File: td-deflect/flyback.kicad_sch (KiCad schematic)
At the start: 38 parts, among them Q12 G3R450MT17J, U13 MCP1416

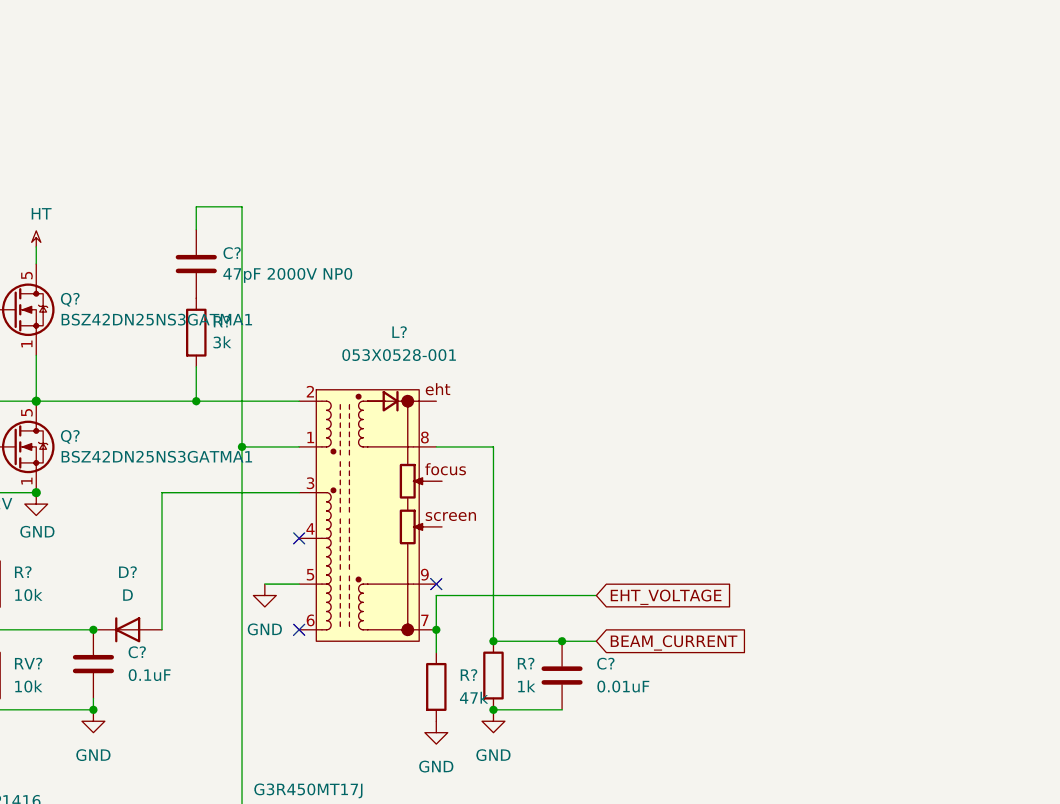
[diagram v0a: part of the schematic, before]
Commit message: modify flyback feedback mechanism
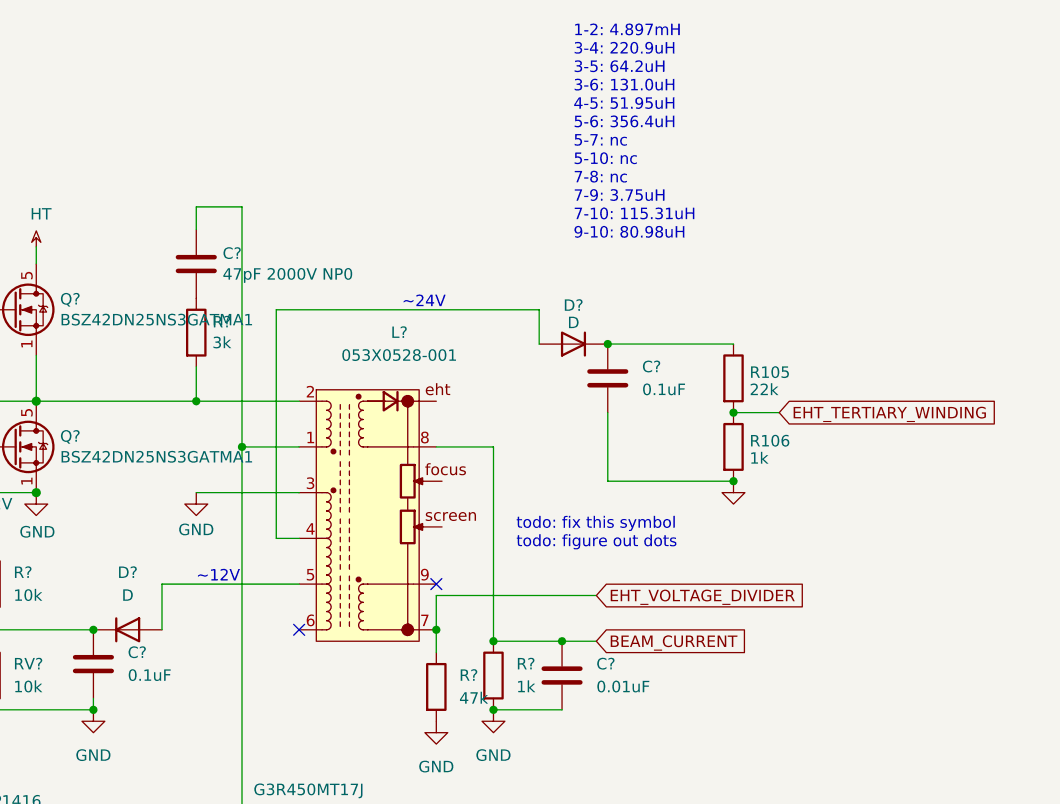
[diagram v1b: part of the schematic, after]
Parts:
- added C?: 0.1uF, symbol Device:C
- added D?: D, symbol Device:D
- added R105: 22k, symbol Device:R
- added R106: 1k, symbol Device:R
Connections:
- net GND: now also L?.3, C?.2, R106.2; no longer L?.5
- net at D?.2 (A): now also L?.5; no longer L?.3
- net at L?.4: now also D?.2 (A)
- net EHT_VOLTAGE renamed EHT_VOLTAGE_DIVIDER
- new net: C?.1, D?.1 (K), R105.1
- new net EHT_TERTIARY_WINDING: R105.2, R106.1
- no-connect marks 3 -> 2
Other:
- note added: "1-2: 4.897mH 3-4: 220.9uH 3-5: 64.2uH 3-6: 131.0uH 4-5: 51.95uH 5-6: 356.4uH 5-7: nc 5-10: nc 7-8: nc 7-9: 3.75uH 7-10: 115.31uH 9-10: 80.98uH"
- note added: "todo: fix this symbol todo: figure out dots"
- note added: "~12V"
- note added: "~24V"

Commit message: more updates
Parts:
- added TP10, TP11, TP4, TP5, TP6, TP7, TP8, TP9: TestPoint, TestPoint:TestPoint_Keystone_5010-5014_Multipurpose, symbol Connector:TestPoint
- C? (x4): footprint (none) -> Capacitor_SMD:C_0805_2012Metric_Pad1.15x1.40mm_HandSolder
- R105, R106, R? (x5): footprint (none) -> Resistor_SMD:R_0805_2012Metric_Pad1.15x1.40mm_HandSolder
- RV?: footprint (none) -> Potentiometer_THT:Potentiometer_Bourns_3386P_Vertical
- U? (x3): footprint (none) -> Package_SO:SOIC-8_3.9x4.9mm_P1.27mm
- U? (x3): footprint (none) -> Package_SO:SOIC-14_3.9x8.7mm_P1.27mm
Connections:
- net BEAM_CURRENT: now also TP6.1
- net EHT_FLYBACK_VOLTAGE: now also TP4.1
- net EHT_VOLTAGE_DIVIDER: now also TP7.1
- net at C?.1, D?.1 (K), U?.2 (-)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: now also TP10.1
- net at R?.2, U?.1, U?.1: now also TP5.1
- net at C?.1, D?.1 (K), R105.1: now also TP9.1
- net at D?.2 (A), L?.4: now also TP8.1
- net at U13.3 (IN), U?.3: now also TP11.1

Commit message: even more updates
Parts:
- L?: footprint (none) -> td-hv:053X0528-001
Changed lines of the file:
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@@
       (effects (font (size 1.27 1.27)))
     )
-    (property "Footprint" "" (at 159.385 61.595 90)
+    (property "Footprint" "td-hv:053X0528-001" (at 159.385 61.595 90)
       (effects (font (size 1.27 1.27)) hide)
     )

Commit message: small bugfix
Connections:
- net EHT_FLYBACK_CURRENT: now also Q12.2 (DS)
- net GND: no longer Q12.2 (DS)
- net HV_PROTECT: now reaches D?.1 (K), U?.1
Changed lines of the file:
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@@
   (junction (at 203.2 118.11) (diameter 0) (color 0 0 0 0)
   )
-  (junction (at 127 120.65) (diameter 0) (color 0 0 0 0)
+  (junction (at 96.52 101.6) (diameter 0) (color 0 0 0 0)
   )
   (junction (at 102.87 113.03) (diameter 0) (color 0 0 0 0)
@@
   )
   (junction (at 171.45 87.63) (diameter 0) (color 0 0 0 0)
+  )
+  (junction (at 142.24 118.11) (diameter 0) (color 0 0 0 0)
   )
   (junction (at 114.3 92.71) (diameter 0) (color 0 0 0 0)
@@
     (stroke (width 0) (type default))
   )
+  (wire (pts (xy 142.24 118.11) (xy 149.86 118.11))
+    (stroke (width 0) (type default))
+  )
   (wire (pts (xy 110.49 49.53) (xy 113.03 49.53))
     (stroke (width 0) (type solid))
@@
     (stroke (width 0) (type default))
   )
-  (wire (pts (xy 127 120.65) (xy 133.35 120.65))
-    (stroke (width 0) (type default))
-  )
   (wire (pts (xy 111.76 104.14) (xy 113.03 104.14))
     (stroke (width 0) (type default))
@@
     (stroke (width 0) (type default))
   )
+  (wire (pts (xy 142.24 115.57) (xy 142.24 118.11))
+    (stroke (width 0) (type default))
+  )
   (wire (pts (xy 100.33 44.45) (xy 105.41 44.45))
     (stroke (width 0) (type solid))
@@
     (stroke (width 0) (type default))
   )
-  (wire (pts (xy 139.7 118.11) (xy 149.86 118.11))
+  (wire (pts (xy 139.7 118.11) (xy 142.24 118.11))
     (stroke (width 0) (type default))
   )
@@
     (stroke (width 0) (type default))
   )
-  (wire (pts (xy 133.35 115.57) (xy 142.24 115.57))
-    (stroke (width 0) (type default))
-  )
   (wire (pts (xy 171.45 87.63) (xy 171.45 90.17))
     (stroke (width 0) (type default))
@@
     (stroke (width 0) (type solid))
   )
-  (wire (pts (xy 133.35 120.65) (xy 133.35 115.57))
-    (stroke (width 0) (type default))
-  )
   (wire (pts (xy 149.86 40.64) (xy 149.86 67.31))
     (stroke (width 0) (type default))
@@
   (wire (pts (xy 127 113.03) (xy 129.54 113.03))
     (stroke (width 0) (type solid))
+  )
+  (wire (pts (xy 63.5 101.6) (xy 96.52 101.6))
+    (stroke (width 0) (type default))
   )
   (wire (pts (xy 189.23 118.11) (xy 189.23 116.84))
@@
     )
   )
+  (global_label "HV_PROTECT" (shape input) (at 63.5 101.6 180) (fields_autoplaced)
+    (effects (font (size 1.27 1.27)) (justify right))
+    (property "Intersheetrefs" "${INTERSHEET_REFS}" (at 49.5576 101.6 0)
+      (effects (font (size 1.27 1.27)) (justify right) hide)
+    )
+  )

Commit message: switch to new 0805 footprint
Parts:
- C19, C? (x6): footprint Capacitor_SMD:C_0805_2012Metric_Pad1.15x1.40mm_HandSolder -> Capacitor_SMD:C_0805_2012Metric_Pad1.18x1.45mm_HandSolder
- D? (x3): footprint (none) -> Diode_SMD:D_0805_2012Metric_Pad1.15x1.40mm_HandSolder
- R105, R106, R33, R34, R35, R36, R42, R? (x7): footprint Resistor_SMD:R_0805_2012Metric_Pad1.15x1.40mm_HandSolder -> Resistor_SMD:R_0805_2012Metric_Pad1.20x1.40mm_HandSolder
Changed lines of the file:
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@@
       (effects (font (size 1.27 1.27)) (justify left))
     )
-    (property "Footprint" "Resistor_SMD:R_0805_2012Metric_Pad1.15x1.40mm_HandSolder" (at 120.142 82.55 90)
+    (property "Footprint" "Resistor_SMD:R_0805_2012Metric_Pad1.20x1.40mm_HandSolder" (at 120.142 82.55 90)
       (effects (font (size 1.27 1.27)) hide)
     )
@@
       (effects (font (size 1.27 1.27)))
     )
-    (property "Footprint" "Resistor_SMD:R_0805_2012Metric_Pad1.15x1.40mm_HandSolder" (at 92.71 95.758 90)
+    (property "Footprint" "Resistor_SMD:R_0805_2012Metric_Pad1.20x1.40mm_HandSolder" (at 92.71 95.758 90)
       (effects (font (size 1.27 1.27)) hide)
     )
@@
       (effects (font (size 1.27 1.27)) (justify left))
     )
-    (property "Footprint" "Capacitor_SMD:C_0805_2012Metric_Pad1.15x1.40mm_HandSolder" (at 78.4352 63.5 0)
+    (property "Footprint" "Capacitor_SMD:C_0805_2012Metric_Pad1.18x1.45mm_HandSolder" (at 78.4352 63.5 0)
       (effects (font (size 1.27 1.27)) hide)
     )
@@
       (effects (font (size 1.27 1.27)) (justify left))
     )
-    (property "Footprint" "Resistor_SMD:R_0805_2012Metric_Pad1.15x1.40mm_HandSolder" (at 202.692 59.69 90)
+    (property "Footprint" "Resistor_SMD:R_0805_2012Metric_Pad1.20x1.40mm_HandSolder" (at 202.692 59.69 90)
       (effects (font (size 1.27 1.27)) hide)
     )
@@
       (effects (font (size 1.27 1.27)))
     )
-    (property "Footprint" "Resistor_SMD:R_0805_2012Metric_Pad1.15x1.40mm_HandSolder" (at 133.35 111.252 90)
+    (property "Footprint" "Resistor_SMD:R_0805_2012Metric_Pad1.20x1.40mm_HandSolder" (at 133.35 111.252 90)
       (effects (font (size 1.27 1.27)) hide)
     )
@@
       (effects (font (size 1.27 1.27)))
     )
-    (property "Footprint" "" (at 137.16 87.63 0)
+    (property "Footprint" "Diode_SMD:D_0805_2012Metric_Pad1.15x1.40mm_HandSolder" (at 137.16 87.63 0)
       (effects (font (size 1.27 1.27)) hide)
     )
@@
       (effects (font (size 1.27 1.27)) (justify right))
     )
-    (property "Footprint" "" (at 96.52 97.79 0)
+    (property "Footprint" "Diode_SMD:D_0805_2012Metric_Pad1.15x1.40mm_HandSolder" (at 96.52 97.79 0)
       (effects (font (size 1.27 1.27)) hide)
     )
@@
       (effects (font (size 1.27 1.27)) (justify left))
     )
-    (property "Footprint" "Resistor_SMD:R_0805_2012Metric_Pad1.15x1.40mm_HandSolder" (at 94.742 86.36 90)
+    (property "Footprint" "Resistor_SMD:R_0805_2012Metric_Pad1.20x1.40mm_HandSolder" (at 94.742 86.36 90)
       (effects (font (size 1.27 1.27)) hide)
     )
@@
       (effects (font (size 1.27 1.27)) (justify left))
     )
-    (property "Footprint" "Resistor_SMD:R_0805_2012Metric_Pad1.15x1.40mm_HandSolder" (at 176.022 92.71 90)
+    (property "Footprint" "Resistor_SMD:R_0805_2012Metric_Pad1.20x1.40mm_HandSolder" (at 176.022 92.71 90)
       (effects (font (size 1.27 1.27)) hide)
     )
@@
       (effects (font (size 1.27 1.27)) (justify left))
     )
-    (property "Footprint" "Capacitor_SMD:C_0805_2012Metric_Pad1.15x1.40mm_HandSolder" (at 97.4852 138.43 0)
+    (property "Footprint" "Capacitor_SMD:C_0805_2012Metric_Pad1.18x1.45mm_HandSolder" (at 97.4852 138.43 0)
       (effects (font (size 1.27 1.27)) hide)
     )
@@
       (effects (font (size 1.27 1.27)) (justify left))
     )
-    (property "Footprint" "Resistor_SMD:R_0805_2012Metric_Pad1.15x1.40mm_HandSolder" (at 169.672 93.98 90)
+    (property "Footprint" "Resistor_SMD:R_0805_2012Metric_Pad1.20x1.40mm_HandSolder" (at 169.672 93.98 90)
       (effects (font (size 1.27 1.27)) hide)
     )
@@
       (effects (font (size 1.27 1.27)) (justify left))
     )
-    (property "Footprint" "Capacitor_SMD:C_0805_2012Metric_Pad1.15x1.40mm_HandSolder" (at 186.3852 96.52 0)
+    (property "Footprint" "Capacitor_SMD:C_0805_2012Metric_Pad1.18x1.45mm_HandSolder" (at 186.3852 96.52 0)
       (effects (font (size 1.27 1.27)) hide)
     )
@@
       (effects (font (size 1.27 1.27)))
     )
-    (property "Footprint" "Resistor_SMD:R_0805_2012Metric_Pad1.15x1.40mm_HandSolder" (at 115.57 65.532 90)
+    (property "Footprint" "Resistor_SMD:R_0805_2012Metric_Pad1.20x1.40mm_HandSolder" (at 115.57 65.532 90)
       (effects (font (size 1.27 1.27)) hide)
     )
@@
       (effects (font (size 1.27 1.27)) (justify left))
     )
-    (property "Footprint" "Capacitor_SMD:C_0805_2012Metric_Pad1.15x1.40mm_HandSolder" (at 84.7852 44.45 0)
+    (property "Footprint" "Capacitor_SMD:C_0805_2012Metric_Pad1.18x1.45mm_HandSolder" (at 84.7852 44.45 0)
       (effects (font (size 1.27 1.27)) hide)
     )
@@
       (effects (font (size 1.27 1.27)) (justify left))
     )
-    (property "Footprint" "Capacitor_SMD:C_0805_2012Metric_Pad1.15x1.40mm_HandSolder" (at 191.4652 63.5 0)
+    (property "Footprint" "Capacitor_SMD:C_0805_2012Metric_Pad1.18x1.45mm_HandSolder" (at 191.4652 63.5 0)
       (effects (font (size 1.27 1.27)) hide)
     )
@@
       (effects (font (size 1.27 1.27)) (justify left))
     )
-    (property "Footprint" "Resistor_SMD:R_0805_2012Metric_Pad1.15x1.40mm_HandSolder" (at 201.422 123.19 90)
+    (property "Footprint" "Resistor_SMD:R_0805_2012Metric_Pad1.20x1.40mm_HandSolder" (at 201.422 123.19 90)
       (effects (font (size 1.27 1.27)) hide)
     )
@@
       (effects (font (size 1.27 1.27)) (justify left))
     )
-    (property "Footprint" "Capacitor_SMD:C_0805_2012Metric_Pad1.15x1.40mm_HandSolder" (at 111.4552 60.96 0)
+    (property "Footprint" "Capacitor_SMD:C_0805_2012Metric_Pad1.18x1.45mm_HandSolder" (at 111.4552 60.96 0)
       (effects (font (size 1.27 1.27)) hide)
     )
@@
       (effects (font (size 1.27 1.27)) (justify left))
     )
-    (property "Footprint" "Resistor_SMD:R_0805_2012Metric_Pad1.15x1.40mm_HandSolder" (at 70.612 116.84 90)
+    (property "Footprint" "Resistor_SMD:R_0805_2012Metric_Pad1.20x1.40mm_HandSolder" (at 70.612 116.84 90)
       (effects (font (size 1.27 1.27)) hide)
     )
@@
       (effects (font (size 1.27 1.27)))
     )
-    (property "Footprint" "" (at 186.69 55.88 0)
+    (property "Footprint" "Diode_SMD:D_0805_2012Metric_Pad1.15x1.40mm_HandSolder" (at 186.69 55.88 0)
       (effects (font (size 1.27 1.27)) hide)
     )
@@
       (effects (font (size 1.27 1.27)) (justify left))
     )
-    (property "Footprint" "Resistor_SMD:R_0805_2012Metric_Pad1.15x1.40mm_HandSolder" (at 148.082 121.92 90)
+    (property "Footprint" "Resistor_SMD:R_0805_2012Metric_Pad1.20x1.40mm_HandSolder" (at 148.082 121.92 90)
       (effects (font (size 1.27 1.27)) hide)
     )
@@
       (effects (font (size 1.27 1.27)))
     )
-    (property "Footprint" "Resistor_SMD:R_0805_2012Metric_Pad1.15x1.40mm_HandSolder" (at 115.57 50.292 90)
+    (property "Footprint" "Resistor_SMD:R_0805_2012Metric_Pad1.20x1.40mm_HandSolder" (at 115.57 50.292 90)
       (effects (font (size 1.27 1.27)) hide)
     )
@@
       (effects (font (size 1.27 1.27)) (justify left))
     )
-    (property "Footprint" "Resistor_SMD:R_0805_2012Metric_Pad1.15x1.40mm_HandSolder" (at 125.222 116.84 90)
+    (property "Footprint" "Resistor_SMD:R_0805_2012Metric_Pad1.20x1.40mm_HandSolder" (at 125.222 116.84 90)
       (effects (font (size 1.27 1.27)) hide)
     )
@@
       (effects (font (size 1.27 1.27)) (justify left))
     )
-    (property "Footprint" "Resistor_SMD:R_0805_2012Metric_Pad1.15x1.40mm_HandSolder" (at 202.692 67.31 90)
+    (property "Footprint" "Resistor_SMD:R_0805_2012Metric_Pad1.20x1.40mm_HandSolder" (at 202.692 67.31 90)
       (effects (font (size 1.27 1.27)) hide)
     )
@@
       (effects (font (size 1.27 1.27)) (justify left))
     )
-    (property "Footprint" "Capacitor_SMD:C_0805_2012Metric_Pad1.15x1.40mm_HandSolder" (at 134.3152 95.25 0)
-      (effects (font (size 1.27 1.27)) hide)
-    )
+    (property "Footprint" "Capacitor_SMD:C_0805_2012Metric_Pad1.18x1.45mm_HandSolder" (at 134.3152 95.25 0)
+      (effects (font (size 1.27 1.27)) hide)
+    )
